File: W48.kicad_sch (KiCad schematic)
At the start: 17 parts, among them P1 R_Potentiometer_Trim, T1 BC847C, T2 BC847C

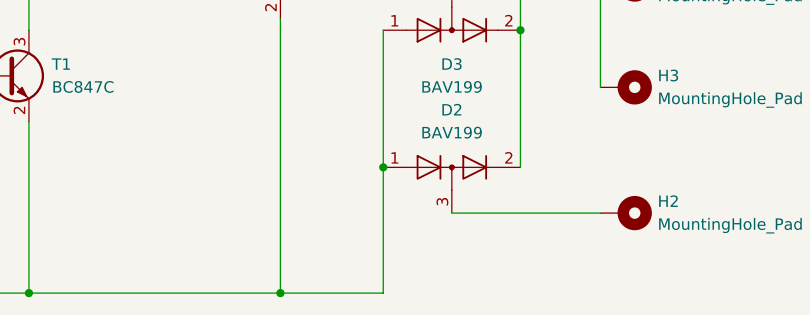
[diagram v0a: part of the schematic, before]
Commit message: real gnd layer
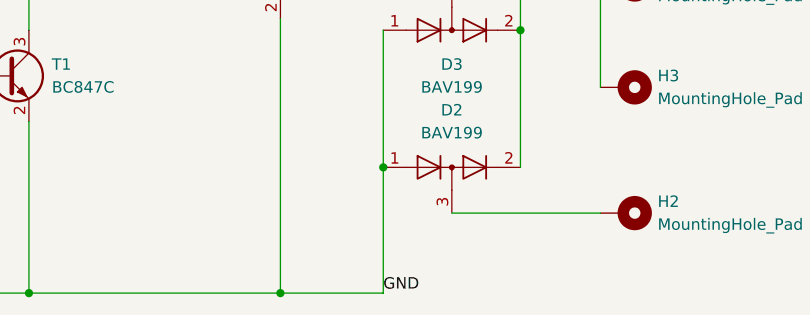
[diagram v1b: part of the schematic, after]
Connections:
- net GND: now reaches C1.2, D1.1 (K), D2.1 (K), D3.1 (K), MK1.1 (-), T1.2 (E), T2.2 (E)
